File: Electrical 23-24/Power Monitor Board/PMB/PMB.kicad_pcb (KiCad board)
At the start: 2 copper layers, 16 parts, among them J1 Conn_01x03_Pin

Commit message: Finish PMB
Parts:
- removed XT60F1: ~, Connector_AMASS:AMASS_XT60PW-F_1x02_P7.20mm_Horizontal
- removed XT60M1: XT60M, Connector_AMASS:AMASS_XT60PW-M_1x02_P7.20mm_Horizontal
- added BATT1: XT60M, PMB:Power, F.Cu at (151.6, 84.8)
- added OUT1: ~, PMB:Power, F.Cu at (162.3, 84.8)
- J1: moved to B.Cu
- moved C1 36.1 mm to (156.8, 106.5), turned to 180 degrees
- moved C2 28.9 mm to (156.2, 100.5), turned to 180 degrees
- moved R2 26.0 mm to (156.8, 103.4)
- moved R6 25.8 mm to (162.9, 100.5), turned to 180 degrees
- moved R7 25.5 mm to (162.9, 99.0)
- moved R3 25.3 mm to (156.8, 104.9), turned to 180 degrees
- moved C4 24.2 mm to (156.2, 99.0), turned to 180 degrees
- moved R4 23.4 mm to (159.5, 99.0)
- moved R5 23.1 mm to (159.5, 100.5), turned to 180 degrees
- moved AP7387-33W5-1 20.8 mm to (157.0, 87.6), turned to -90 degrees
- moved C3 19.8 mm to (157.0, 84.4), turned to 180 degrees
- moved R1 11.0 mm to (157.0, 94.0)
- moved J1 8.91 mm to (151.8, 100.7), turned to -90 degrees
- moved MCP6007T1 1.52 mm to (161.2, 104.3), turned to -90 degrees
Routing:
- net /BATT: track 0.00 -> 47.8 mm, vias 0 -> 26
- net /GND: track 0.00 -> 28.4 mm, vias 0 -> 40
- net /3V3: track 0.00 -> 25.8 mm, vias 0 -> 2
- net /VM: track 0.00 -> 19.0 mm
- net /GND2: track 0.00 -> 16.8 mm, vias 0 -> 34
- net /CM: track 0.00 -> 16.7 mm
- net /VDIV: track 0.00 -> 5.73 mm
- net Net-(MCP6007T1-+-Pad3): track 0.00 -> 3.38 mm
- net Net-(MCP6007T1---Pad2): track 0.00 -> 3.37 mm
- added copper zone on B.Cu, net /GND
- added copper zone on B.Cu, net /GND2
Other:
- board outline added: 16.8 x 29.5 mm
- board text added: "2xOPAMP"
- board text added: "BATT"
- board text added: "LDO"
- board text added: "OUT"

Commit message: Final PMB
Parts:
- removed C4: 10uF, Capacitor_SMD:C_0603_1608Metric_Pad1.08x0.95mm_HandSolder
- added G***: LOGO, LOGO, B.Cu at (157.1, 88.7)
- BATT1: value XT60M -> 10AWG_1x02
- J1: value Conn_01x03_Pin -> JST_XH_04; footprint Connector_JST:JST_XH_S3B-XH-A_1x03_P2.50mm_Horizontal -> Connector_JST:JST_XH_S4B-XH-A_1x04_P2.50mm_Horizontal
- OUT1: value ~ -> 10AWG_1x02
- R2: value 150k -> 180k
- R5, R7: value 680k -> 620k
- moved C2 2.27 mm to (154.4, 99.1)
- moved R2 1.22 mm to (156.0, 102.5), turned to -90 degrees
- moved R4 0.79 mm to (158.8, 99.0)
- moved R5 0.78 mm to (158.8, 100.5)
- moved R6 0.62 mm to (162.3, 100.5)
- moved R7 0.62 mm to (162.3, 99.0)
- moved R1 0.08 mm to (157.0, 94.1)
- moved OUT1 0.06 mm to (162.3, 84.9)
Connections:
- J1 pad 2: /CM -> /GND
- J1 pad 3: /GND -> /CM
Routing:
- net /3V3: track 25.8 -> 40.6 mm, vias 2 -> 0
- net /BATT: track 47.8 -> 43.2 mm, vias 26 -> 24
- net /GND: track 28.4 -> 24.3 mm
- net /VM: track 19.0 -> 22.3 mm
- net /GND2: track 16.8 -> 15.9 mm, vias 34 -> 33
- net /VDIV: track 5.73 -> 6.57 mm
- net Net-(MCP6007T1-+-Pad3): track 3.38 -> 3.90 mm
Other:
- board size 16.8 x 29.5 mm -> 16.8 x 32.3 mm
- board text added: "3/15/24"
- board text added: "Ari B Solomiia K"
- board text added: "DUAL OPAMP"
- board text added: "MCP 6007"
- board text added: "VM GND CM GND JST-XH"
- board text removed: "2xOPAMP"

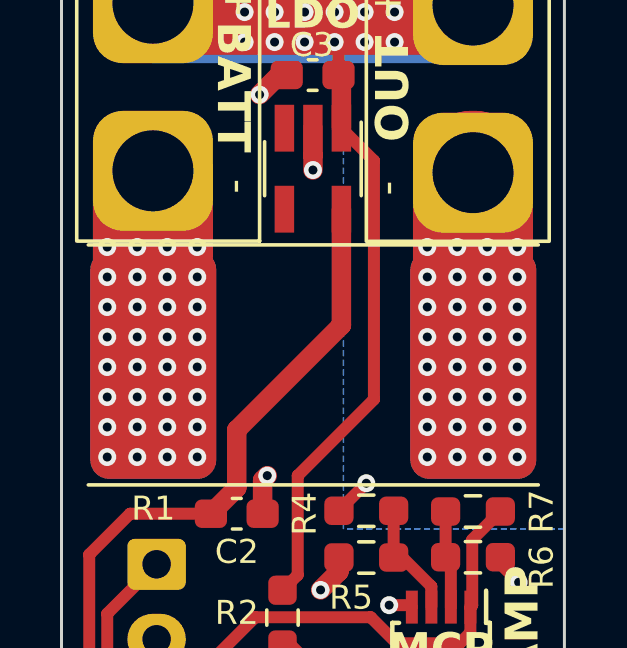
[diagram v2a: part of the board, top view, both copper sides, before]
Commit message: Add JLC Serial # Location to All
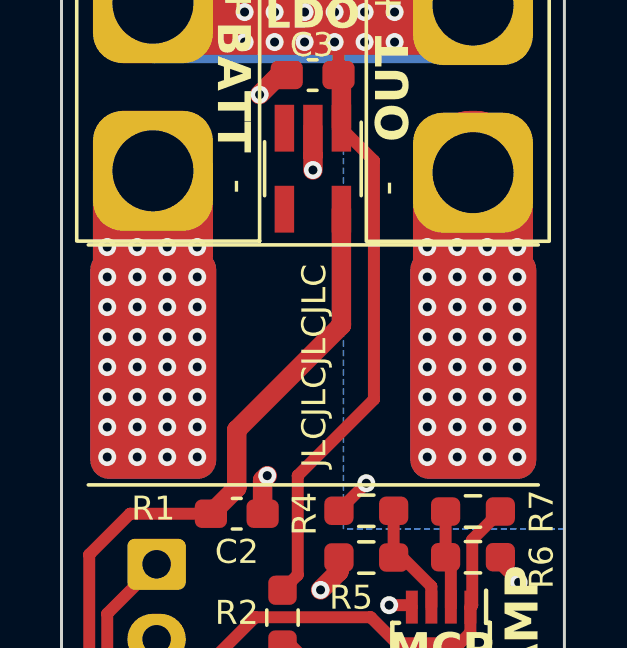
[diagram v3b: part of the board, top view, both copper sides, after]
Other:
- board text added: "JLCJLCJLCJLC"
